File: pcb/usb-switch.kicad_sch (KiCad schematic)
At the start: 5 parts, among them U12 FSUSB42UMX

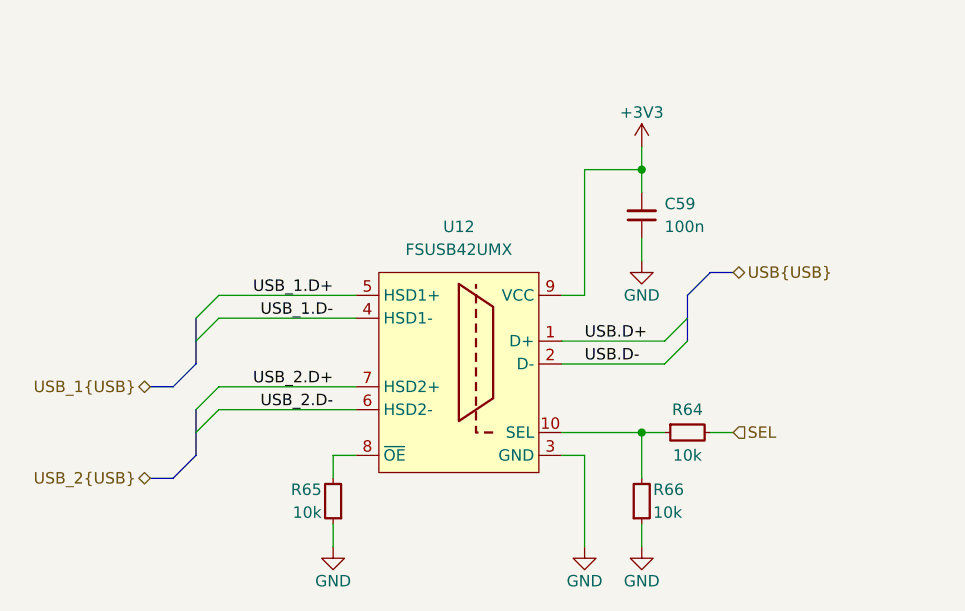
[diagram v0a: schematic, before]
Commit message: [#5] Refactor the schematic
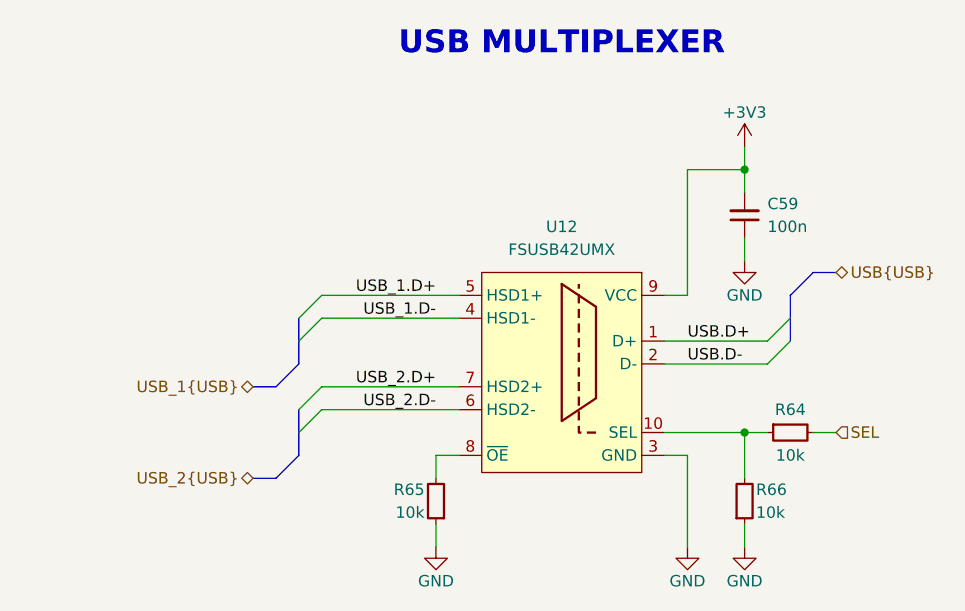
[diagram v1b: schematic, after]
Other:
- note added: "USB MULTIPLEXER"
- moved on the sheet: C59, R64, R65, R66, U12
